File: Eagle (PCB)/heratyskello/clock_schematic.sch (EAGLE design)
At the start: 22 parts, among them IC1 DS3231/SO

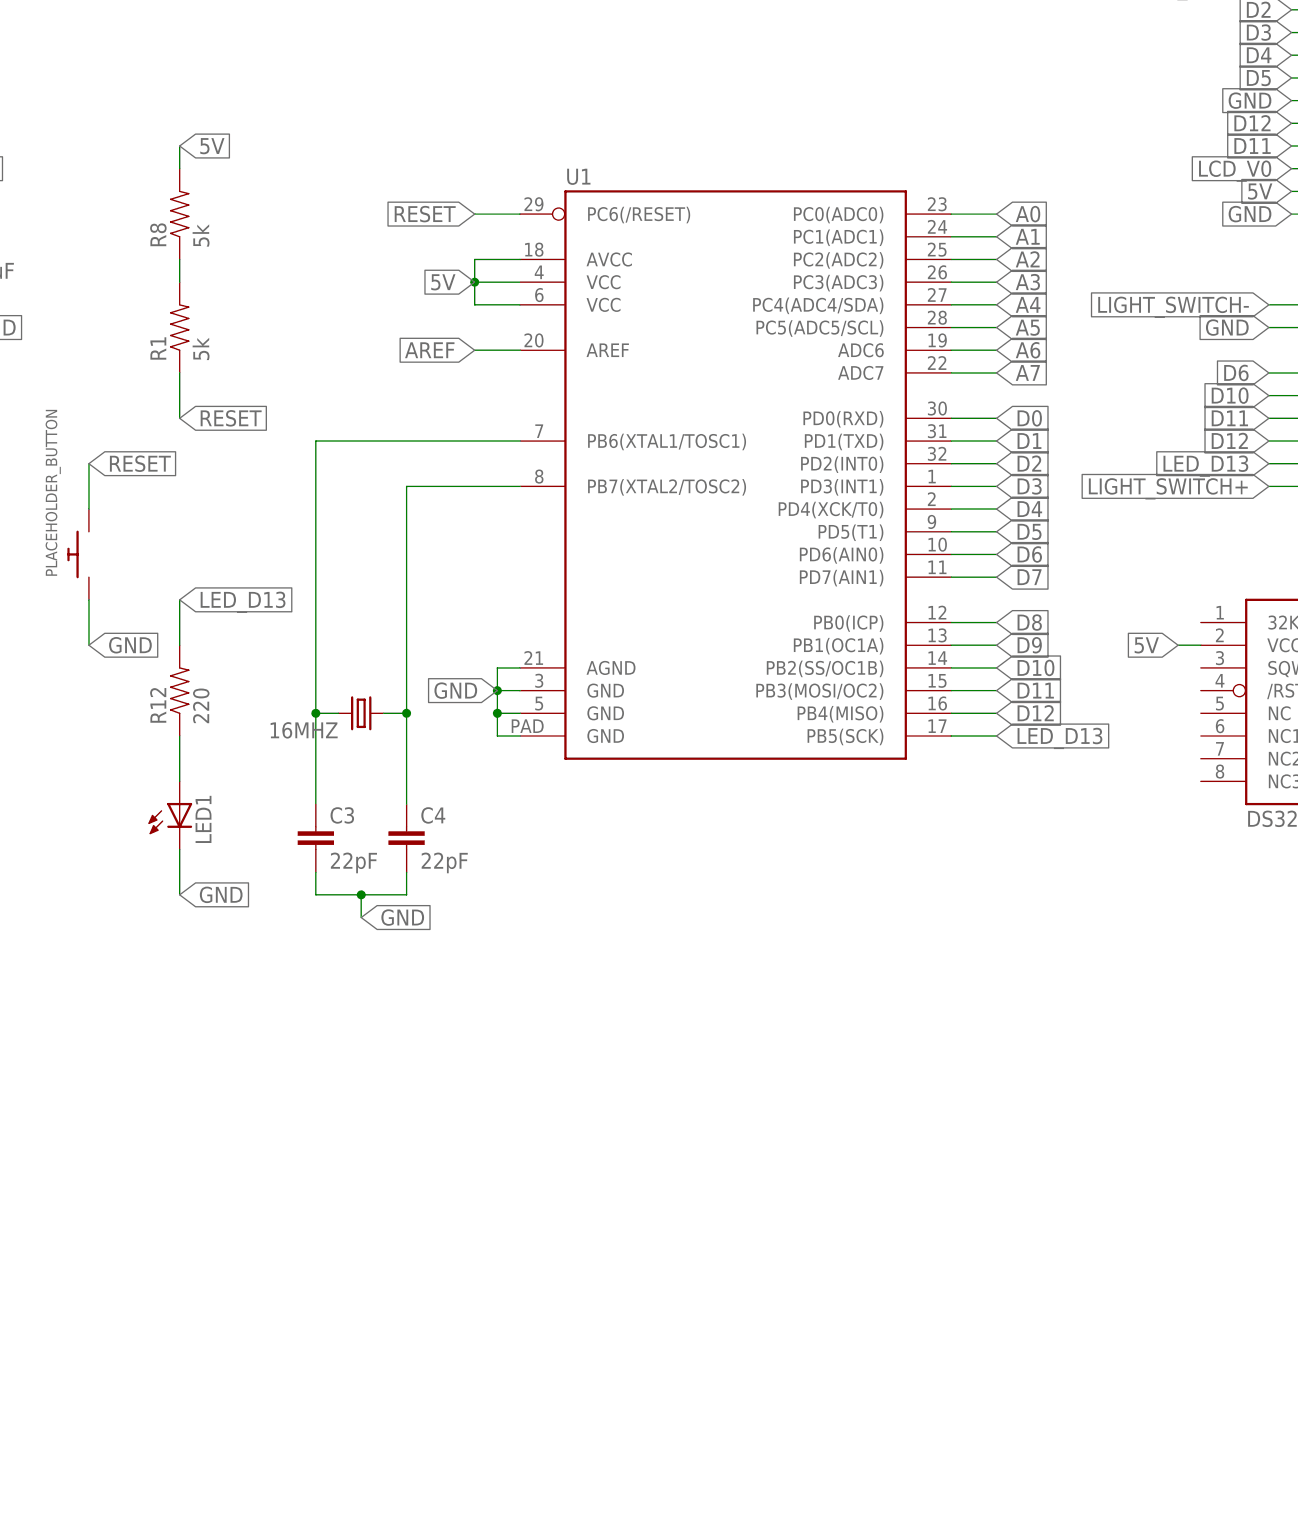
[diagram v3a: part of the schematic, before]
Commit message: Eagle Fuckup Corrected
Atmega is now the correct size.
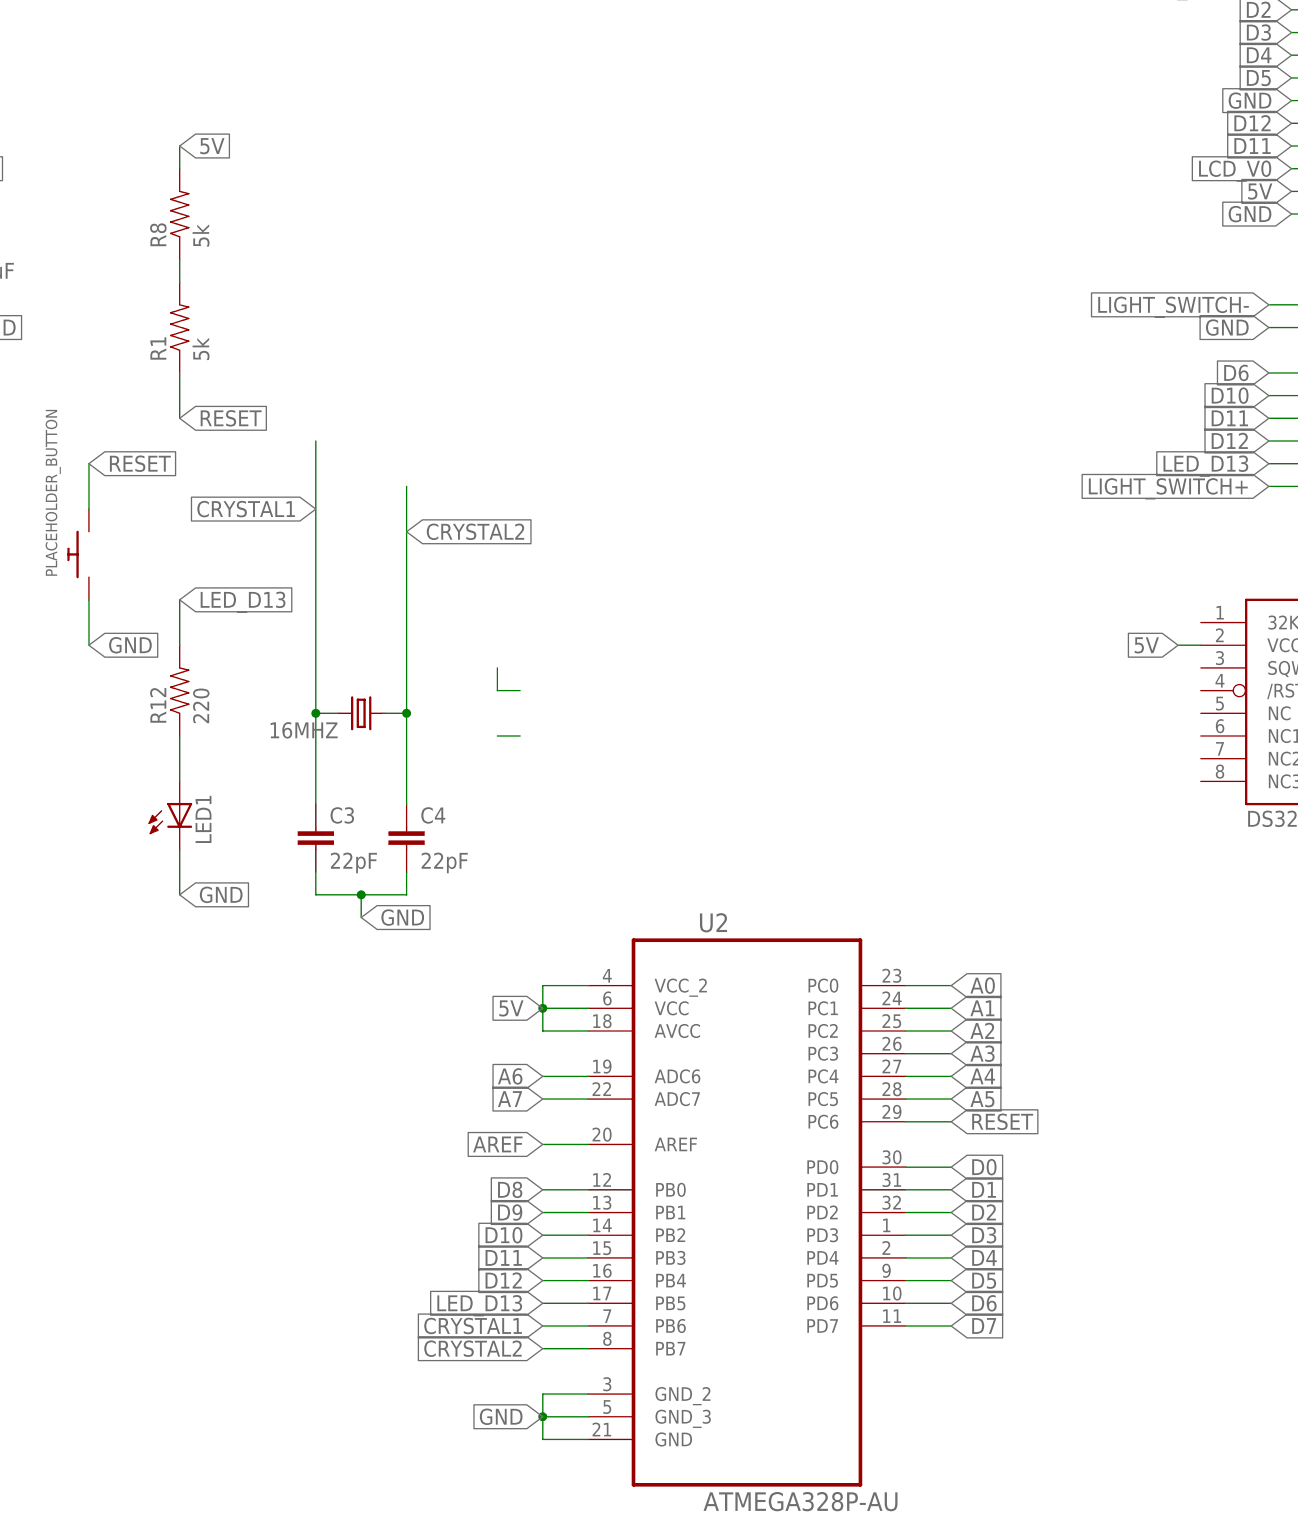
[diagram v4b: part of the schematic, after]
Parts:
- removed U1: (no value), SparkFun-DigitalIC:ATMEGA328P_MLFMLF32
- added U2: ATMEGA328P-AU, Atmel_By_element14_Batch_1-00:ATMEGA328P-AU
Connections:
- removed net N$1: 16MHZ.2, C3.1, U1.PB6(XTAL1/TOSC1)
- removed net N$2: 16MHZ.1, C4.1, U1.PB7(XTAL2/TOSC2)
- new net CRYSTAL1: 16MHZ.2, C3.1, U2.PB6
- new net CRYSTAL2: 16MHZ.1, C4.1, U2.PB7
- net 5V: now also U2.AVCC, U2.VCC, U2.VCC_2; no longer U1.AVCC, U1.VCC@4, U1.VCC@6
- net A0: now also U2.PC0; no longer U1.PC0(ADC0)
- net A1: now also U2.PC1; no longer U1.PC1(ADC1)
- net A2: now also U2.PC2; no longer U1.PC2(ADC2)
- net A3: now also U2.PC3; no longer U1.PC3(ADC3)
- net A4: now also U2.PC4; no longer U1.PC4(ADC4/SDA)
- net A5: now also U2.PC5; no longer U1.PC5(ADC5/SCL)
- net A6: now also U2.ADC6; no longer U1.ADC6
- net A7: now also U2.ADC7; no longer U1.ADC7
- net AREF: now also U2.AREF; no longer U1.AREF
- net D0: now also U2.PD0; no longer U1.PD0(RXD)
- net D1: now also U2.PD1; no longer U1.PD1(TXD)
- net D10: now also U2.PB2; no longer U1.PB2(SS/OC1B)
- net D11: now also U2.PB3; no longer U1.PB3(MOSI/OC2)
- net D12: now also U2.PB4; no longer U1.PB4(MISO)
- net D2: now also U2.PD2; no longer U1.PD2(INT0)
- net D3: now also U2.PD3; no longer U1.PD3(INT1)
- net D4: now also U2.PD4; no longer U1.PD4(XCK/T0)
- net D5: now also U2.PD5; no longer U1.PD5(T1)
- net D6: now also U2.PD6; no longer U1.PD6(AIN0)
- net D7: now also U2.PD7; no longer U1.PD7(AIN1)
- net D8: now also U2.PB0; no longer U1.PB0(ICP)
- net D9: now also U2.PB1; no longer U1.PB1(OC1A)
- net GND: now also U2.GND, U2.GND_2, U2.GND_3; no longer U1.AGND, U1.GND@3, U1.GND@5, U1.GND@PAD
- net LED_D13: now also U2.PB5; no longer U1.PB5(SCK)
- net RESET: now also U2.PC6; no longer U1.PC6(/RESET)
